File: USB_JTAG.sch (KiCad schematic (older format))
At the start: 31 parts, among them J4 USB_B_Micro, J5 AVR-JTAG-10, U11 5M1270ZT144C5N, U12 93LC46BT-I/OT, U8 FT2232H, U9 TPD2EUSB30, X1 KC5032K12.0000C10E00

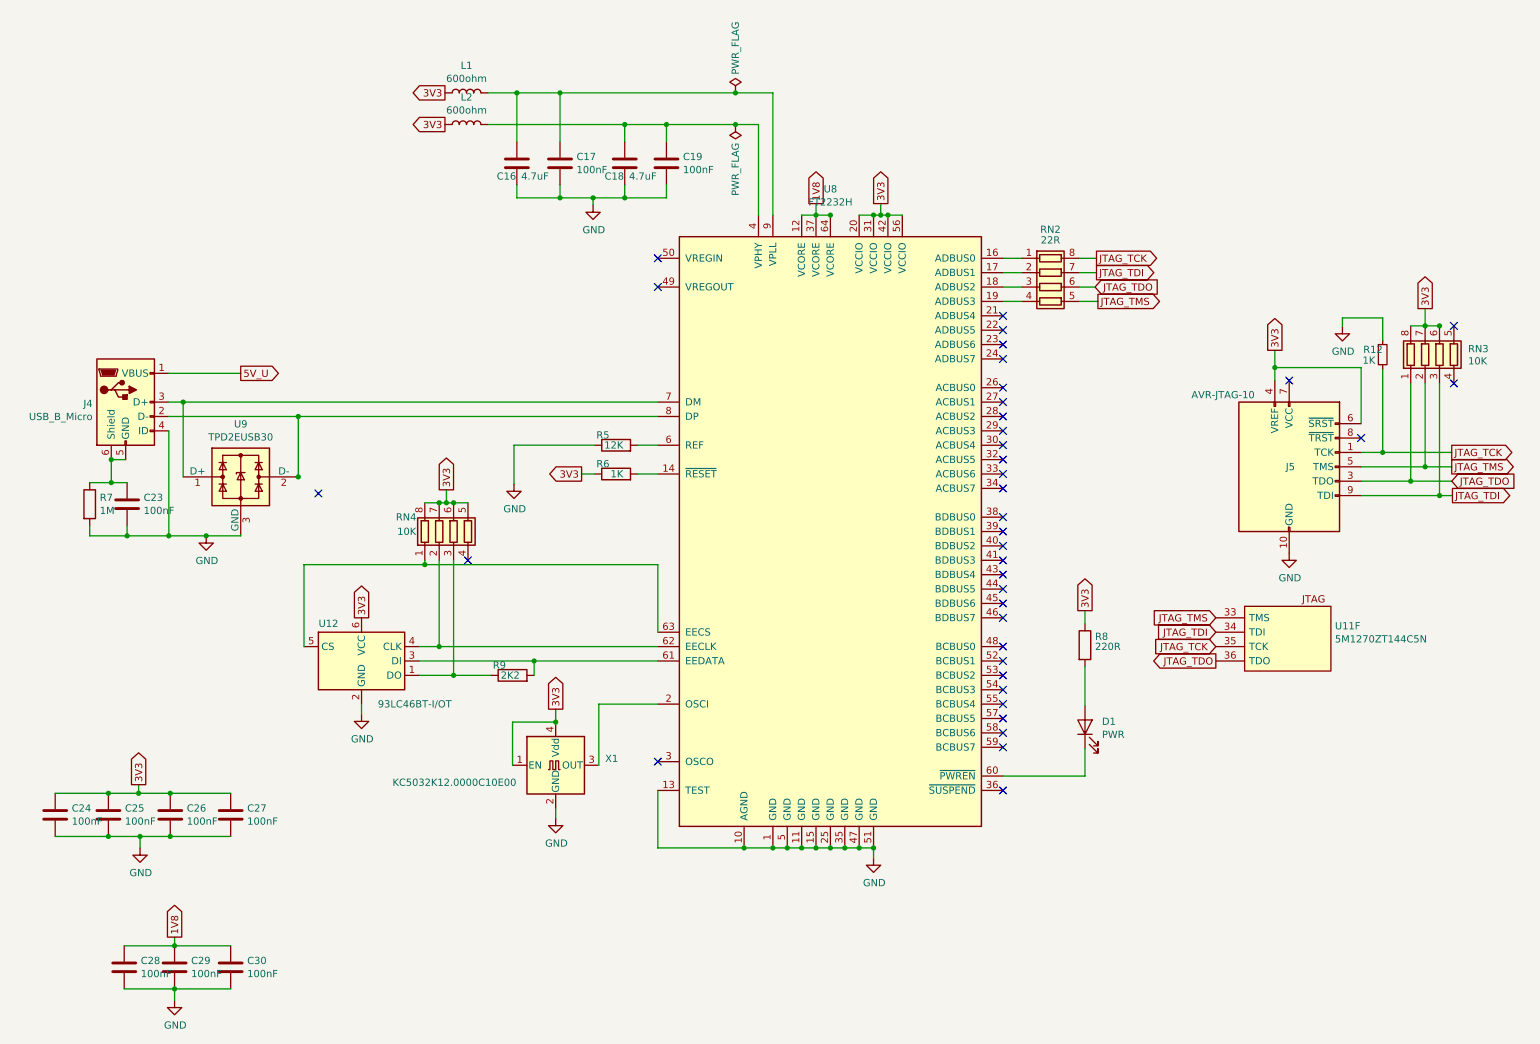
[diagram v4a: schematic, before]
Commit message: replaced some global pins with hierarchical sheet pins
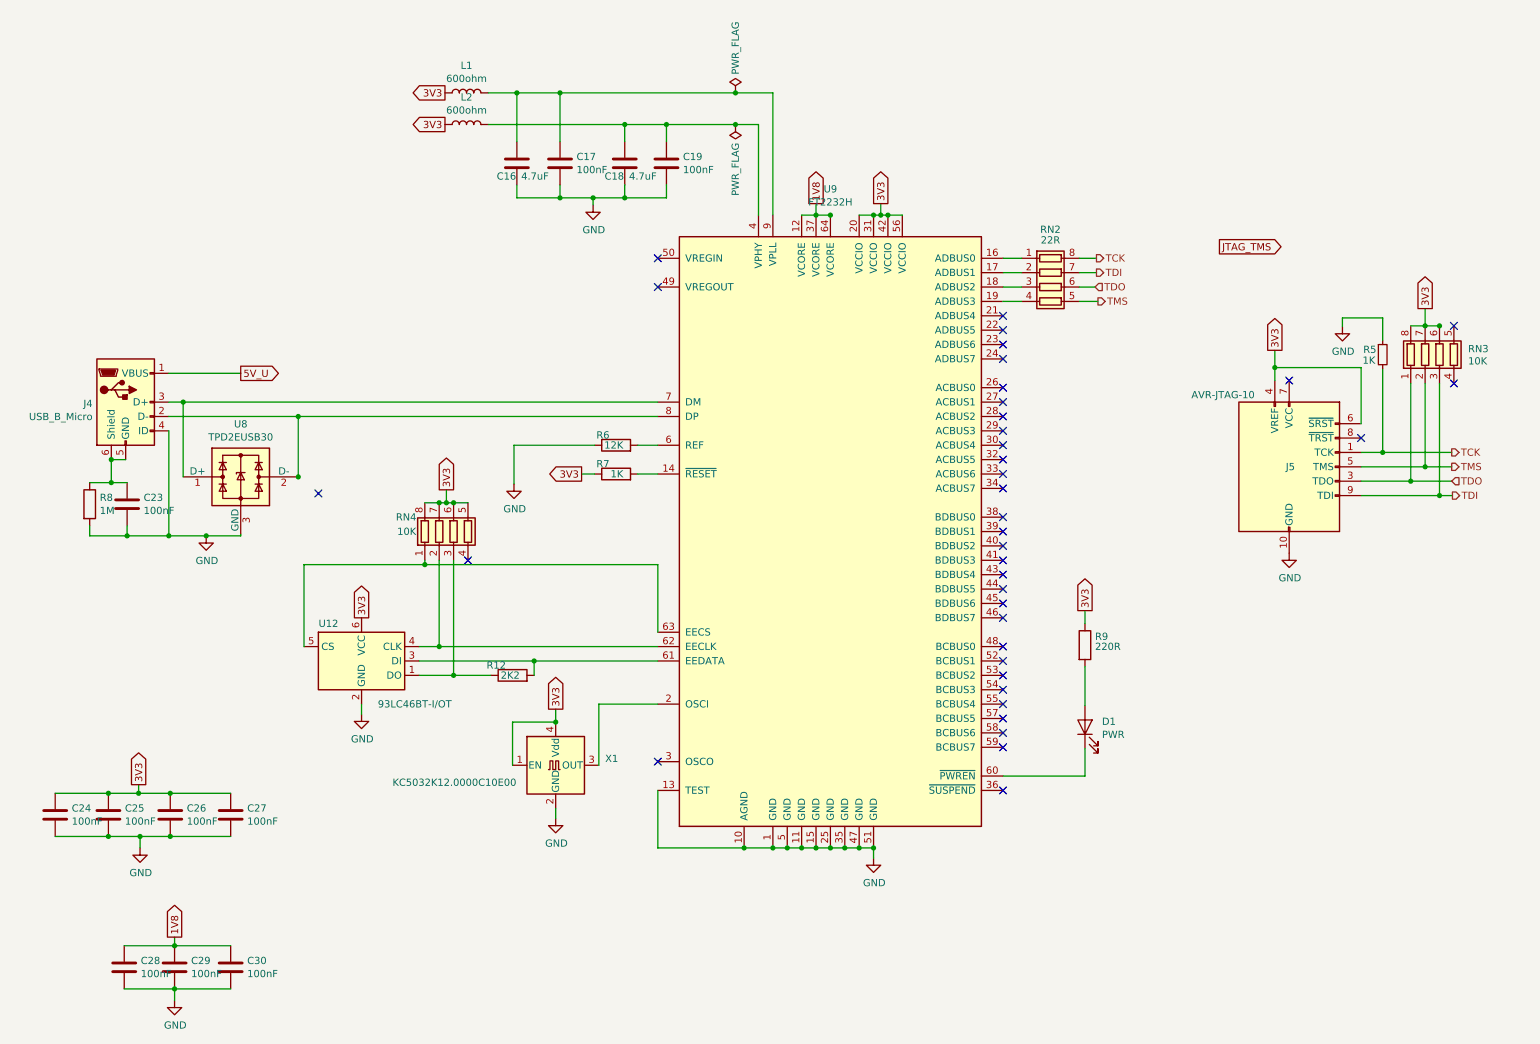
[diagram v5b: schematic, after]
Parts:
- removed U11: 5M1270ZT144C5N, Package_QFP:TQFP-144_20x20mm_P0.5mm, symbol rc2014_max_v-rescue:5M1270ZT144C5N-CPLD_Altera
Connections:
- net JTAG_TMS: no longer J5.5 (TMS), RN2.5 (R4.2), RN3.2 (R2.1)
- net JTAG_TCK renamed TCK
- net JTAG_TDI renamed TDI
- net JTAG_TDO renamed TDO
- new net TMS: J5.5 (TMS), RN2.5 (R4.2), RN3.2 (R2.1)

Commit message: recovered layout
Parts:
- X1: symbol Oscillator:KC5032K12.0000C10E00 -> rc2014_max_v-rescue:KC5032K12.0000C10E00-Oscillator
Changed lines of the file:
@@
 	1    0    0    1
 $EndComp
-Text GLabel 8905 2050 2    50   Output ~ 0
-JTAG_TMS
 Text GLabel 2100 2930 2    50   Output ~ 0
 5V_U
@@
 NoConn ~ 5000 5630
 $Comp
-L Oscillator:KC5032K12.0000C10E00 X1
+L rc2014_max_v-rescue:KC5032K12.0000C10E00-Oscillator X1
 U 1 1 5D18454F
 P 4290 5655
 AR Path="/5D0F9837/5D18454F" Ref="X1"  Part="1"
 AR Path="/5CFABACD/5D0BF766/5D18454F" Ref="X1"  Part="1"
+AR Path="/5D18454F" Ref="X1"  Part="1"
 F 0 "X1" H 4634 5701 50  0000 L CNN
 F 1 "KC5032K12.0000C10E00" H 3155 5535 50  0000 L CNN

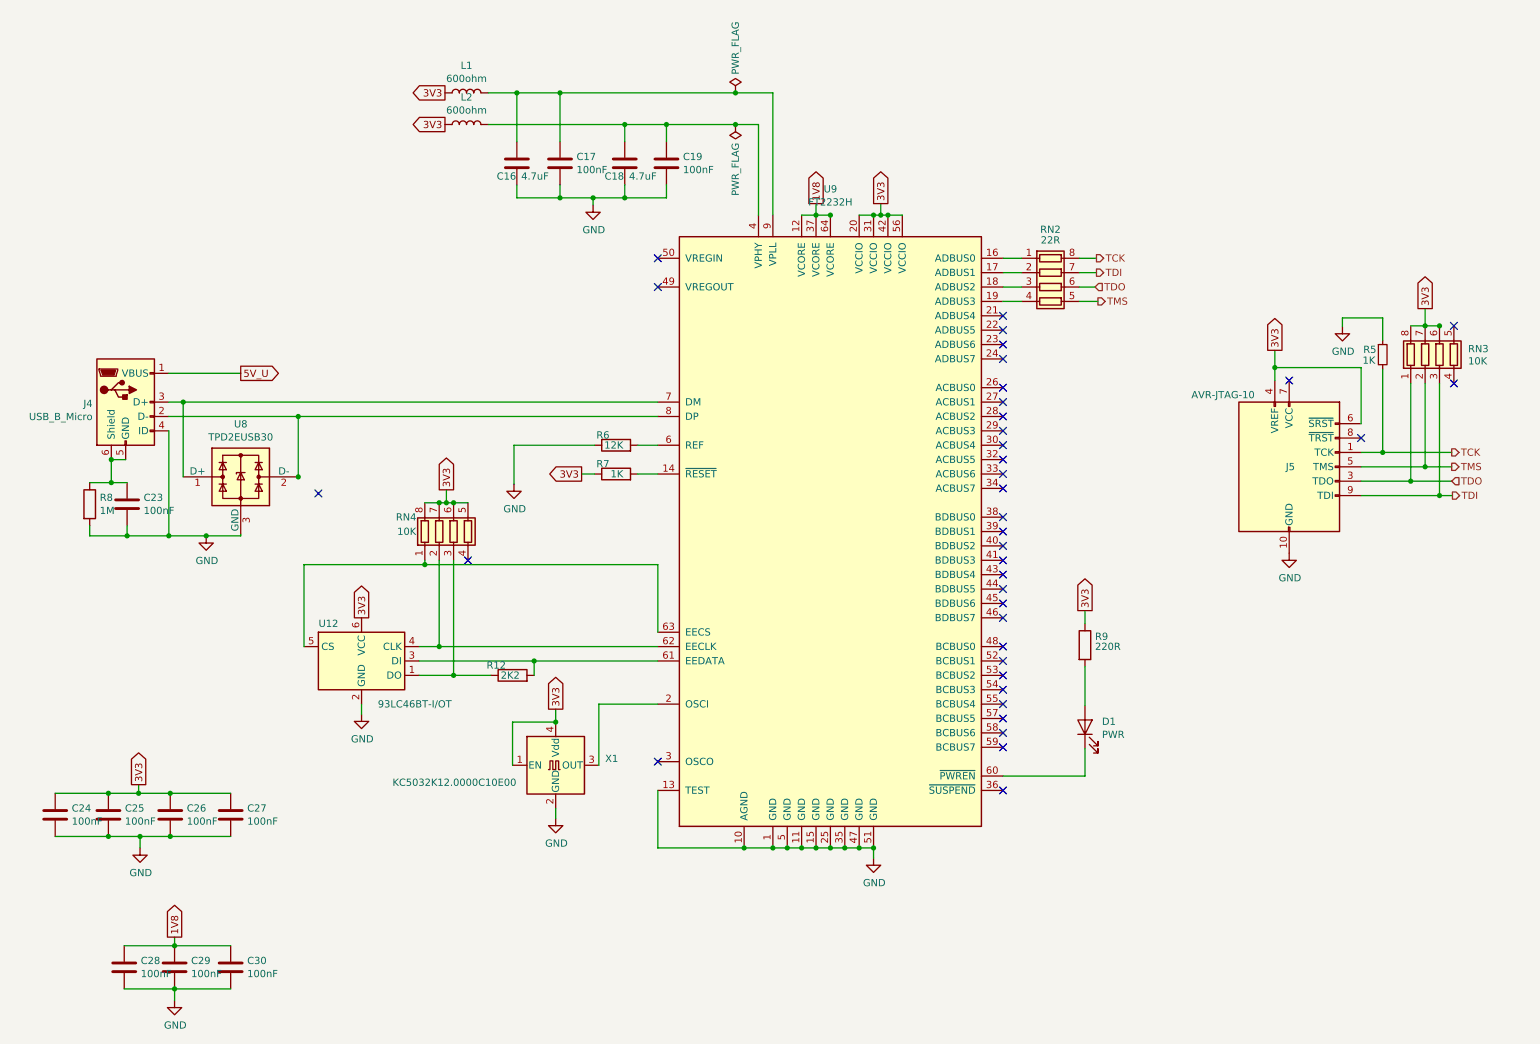
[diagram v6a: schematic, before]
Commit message: Added bus structure, additional pins added, 5V load balancer
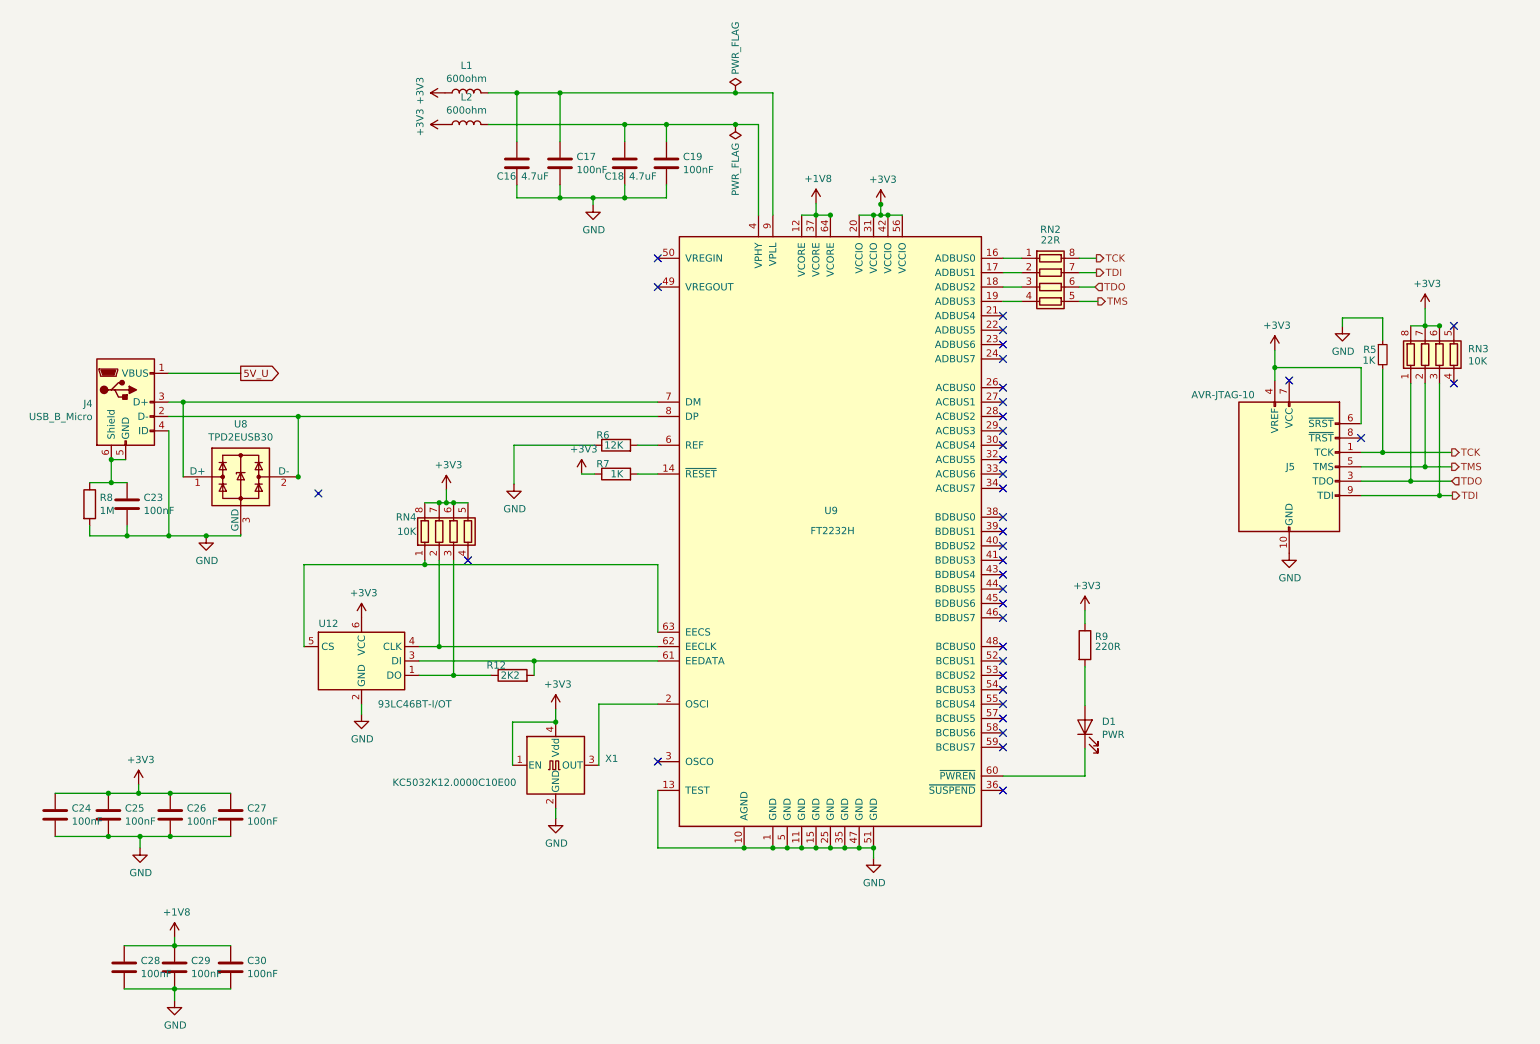
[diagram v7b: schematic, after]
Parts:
- J5: footprint Connector_IDC:IDC-Header_2x05_P2.54mm_Horizontal -> Connector_PinHeader_1.27mm:PinHeader_2x05_P1.27mm_Vertical
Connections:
- net labels added: +1V8, +3V3
- net labels removed: 1V8, 3V3
- wire segments 145 -> 146
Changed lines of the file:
@@
 EESchema Schematic File Version 4
 LIBS:rc2014_max_v-cache
+LIBS:sbc_z80-cache
+LIBS:power_share-cache
 EELAYER 29 0
 EELAYER END
@@
 F 0 "J5" H 9430 3580 50  0000 R CNN
 F 1 "AVR-JTAG-10" H 9150 4080 50  0000 R CNN
-F 2 "Connector_IDC:IDC-Header_2x05_P2.54mm_Horizontal" V 9240 3730 50  0001 C CNN
+F 2 "Connector_PinHeader_1.27mm:PinHeader_2x05_P1.27mm_Vertical" V 9240 3730 50  0001 C CNN
 F 3 "~" H 8115 3030 50  0001 C CNN
 	1    9390 3580
@@
 AR Path="/5D0F9837/5D013565" Ref="U8"  Part="1"
 AR Path="/5CFABACD/5D0BF766/5D013565" Ref="U9"  Part="1"
-F 0 "U9" H 6200 6411 50  0000 C CNN
-F 1 "FT2232H" H 6200 6320 50  0000 C CNN
+F 0 "U9" H 6205 4175 50  0000 C CNN
+F 1 "FT2232H" H 6215 4035 50  0000 C CNN
 F 2 "Package_QFP:TQFP-64_10x10mm_P0.5mm" H 6200 4030 50  0001 C CNN
 F 3 "https://www.mouser.com/datasheet/2/163/DS_FT2232H-17353.pdf" H 6200 4030 50  0001 C CNN
@@
 Text GLabel 2100 2930 2    50   Output ~ 0
 5V_U
-Text GLabel 6550 1750 1    50   Output ~ 0
-3V3
-Text GLabel 6100 1750 1    50   Output ~ 0
-1V8
-Text GLabel 3520 980  0    50   Output ~ 0
-3V3
-Text GLabel 3520 1200 0    50   Output ~ 0
-3V3
-Text GLabel 3530 3740 1    50   Output ~ 0
-3V3
-Text GLabel 10335 2480 1    50   Output ~ 0
-3V3
-Text GLabel 9290 2770 1    50   Output ~ 0
-3V3
-Text GLabel 7970 4580 1    50   Output ~ 0
-3V3
-Text GLabel 1390 5790 1    50   Output ~ 0
-3V3
-Text GLabel 1640 6850 1    50   Output ~ 0
-1V8
-Text GLabel 2940 4630 1    50   Output ~ 0
-3V3
-Text GLabel 4470 3630 0    50   Output ~ 0
-3V3
 Wire Wire Line
 	5000 5830 5000 6230
@@
 	6100 1830 6100 1750
 Wire Wire Line
-	6550 1830 6550 1750
+	6550 1830 6550 1755
 Wire Wire Line
 	1600 3130 1700 3130
@@
 Wire Wire Line
 	3990 5355 4290 5355
-Text GLabel 4290 5265 1    50   Output ~ 0
-3V3
 Wire Wire Line
 	4290 5265 4290 5355
@@
 Text HLabel 10520 3580 2    50   Output ~ 0
 TMS
+$Comp
+L power:+3V3 #PWR?
+U 1 1 5D9343EB
+P 4470 3630
+AR Path="/5D9343EB" Ref="#PWR?"  Part="1"
+AR Path="/5CFABACD/5D0BF766/5D9343EB" Ref="#PWR060"  Part="1"
+F 0 "#PWR060" H 4470 3480 50  0001 C CNN
+F 1 "+3V3" H 4485 3803 50  0000 C CNN
+F 2 "" H 4470 3630 50  0001 C CNN
+F 3 "" H 4470 3630 50  0001 C CNN
+	1    4470 3630
+	1    0    0    -1
+$EndComp
+$Comp
+L power:+3V3 #PWR?
+U 1 1 5D94566F
+P 3530 3740
+AR Path="/5D94566F" Ref="#PWR?"  Part="1"
+AR Path="/5CFABACD/5D0BF766/5D94566F" Ref="#PWR062"  Part="1"
+F 0 "#PWR062" H 3530 3590 50  0001 C CNN
+F 1 "+3V3" H 3545 3913 50  0000 C CNN
+F 2 "" H 3530 3740 50  0001 C CNN
+F 3 "" H 3530 3740 50  0001 C CNN
+	1    3530 3740
+	1    0    0    -1
+$EndComp
+$Comp
+L power:+3V3 #PWR?
+U 1 1 5D956672
+P 2940 4630
+AR Path="/5D956672" Ref="#PWR?"  Part="1"
+AR Path="/5CFABACD/5D0BF766/5D956672" Ref="#PWR064"  Part="1"
+F 0 "#PWR064" H 2940 4480 50  0001 C CNN
+F 1 "+3V3" H 2955 4803 50  0000 C CNN
+F 2 "" H 2940 4630 50  0001 C CNN
+F 3 "" H 2940 4630 50  0001 C CNN
+	1    2940 4630
+	1    0    0    -1
+$EndComp
+$Comp
+L power:+3V3 #PWR?
+U 1 1 5D9675DE
+P 4290 5265
+AR Path="/5D9675DE" Ref="#PWR?"  Part="1"
+AR Path="/5CFABACD/5D0BF766/5D9675DE" Ref="#PWR065"  Part="1"
+F 0 "#PWR065" H 4290 5115 50  0001 C CNN
+F 1 "+3V3" H 4305 5438 50  0000 C CNN
+F 2 "" H 4290 5265 50  0001 C CNN
+F 3 "" H 4290 5265 50  0001 C CNN
+	1    4290 5265
+	1    0    0    -1
+$EndComp
+$Comp
+L power:+3V3 #PWR?
+U 1 1 5D9784C6
+P 1390 5790
+AR Path="/5D9784C6" Ref="#PWR?"  Part="1"
+AR Path="/5CFABACD/5D0BF766/5D9784C6" Ref="#PWR067"  Part="1"
+F 0 "#PWR067" H 1390 5640 50  0001 C CNN
+F 1 "+3V3" H 1405 5963 50  0000 C CNN
+F 2 "" H 1390 5790 50  0001 C CNN
+F 3 "" H 1390 5790 50  0001 C CNN
+	1    1390 5790
+	1    0    0    -1
+$EndComp
+$Comp
+L power:+1V8 #PWR068
+U 1 1 5D9891A4
+P 1640 6850
+F 0 "#PWR068" H 1640 6700 50  0001 C CNN
+F 1 "+1V8" H 1655 7023 50  0000 C CNN
+F 2 "" H 1640 6850 50  0001 C CNN
+F 3 "" H 1640 6850 50  0001 C CNN
+	1    1640 6850
+	1    0    0    -1
+$EndComp
+$Comp
+L power:+3V3 #PWR?
+U 1 1 5D995718
+P 6550 1755
+AR Path="/5D995718" Ref="#PWR?"  Part="1"
+AR Path="/5CFABACD/5D0BF766/5D995718" Ref="#PWR057"  Part="1"
+F 0 "#PWR057" H 6550 1605 50  0001 C CNN
+F 1 "+3V3" H 6565 1928 50  0000 C CNN
+F 2 "" H 6550 1755 50  0001 C CNN
+F 3 "" H 6550 1755 50  0001 C CNN
+	1    6550 1755
+	1    0    0    -1
+$EndComp
+Connection ~ 6550 1755
+Wire Wire Line
+	6550 1755 6550 1750
+$Comp
+L power:+3V3 #PWR?
+U 1 1 5D9AC54D
+P 9290 2770
+AR Path="/5D9AC54D" Ref="#PWR?"  Part="1"
+AR Path="/5CFABACD/5D0BF766/5D9AC54D" Ref="#PWR059"  Part="1"
+F 0 "#PWR059" H 9290 2620 50  0001 C CNN
+F 1 "+3V3" H 9305 2943 50  0000 C CNN
+F 2 "" H 9290 2770 50  0001 C CNN
+F 3 "" H 9290 2770 50  0001 C CNN
+	1    9290 2770
+	1    0    0    -1
+$EndComp
+$Comp
+L power:+3V3 #PWR?
+U 1 1 5D9B1E4B
+P 10335 2480
+AR Path="/5D9B1E4B" Ref="#PWR?"  Part="1"
+AR Path="/5CFABACD/5D0BF766/5D9B1E4B" Ref="#PWR058"  Part="1"
+F 0 "#PWR058" H 10335 2330 50  0001 C CNN
+F 1 "+3V3" H 10350 2653 50  0000 C CNN
+F 2 "" H 10335 2480 50  0001 C CNN
+F 3 "" H 10335 2480 50  0001 C CNN
+	1    10335 2480
+	1    0    0    -1
+$EndComp
+$Comp
+L power:+3V3 #PWR?
+U 1 1 5D9D4519
+P 3520 980
+AR Path="/5D9D4519" Ref="#PWR?"  Part="1"
+AR Path="/5CFABACD/5D0BF766/5D9D4519" Ref="#PWR054"  Part="1"
+F 0 "#PWR054" H 3520 830 50  0001 C CNN
+F 1 "+3V3" H 3535 1153 50  0000 C CNN
+F 2 "" H 3520 980 50  0001 C CNN
+F 3 "" H 3520 980 50  0001 C CNN
+	1    3520 980
+	0    -1   -1   0
+$EndComp
+$Comp
+L power:+3V3 #PWR?
+U 1 1 5D9DFE3B
+P 3520 1200
+AR Path="/5D9DFE3B" Ref="#PWR?"  Part="1"
+AR Path="/5CFABACD/5D0BF766/5D9DFE3B" Ref="#PWR055"  Part="1"
+F 0 "#PWR055" H 3520 1050 50  0001 C CNN
+F 1 "+3V3" H 3535 1373 50  0000 C CNN
+F 2 "" H 3520 1200 50  0001 C CNN
+F 3 "" H 3520 1200 50  0001 C CNN
+	1    3520 1200
+	0    -1   -1   0
+$EndComp
+$Comp
+L power:+1V8 #PWR056
+U 1 1 5D9EC038
+P 6100 1750
+F 0 "#PWR056" H 6100 1600 50  0001 C CNN
+F 1 "+1V8" H 6115 1923 50  0000 C CNN
+F 2 "" H 6100 1750 50  0001 C CNN
+F 3 "" H 6100 1750 50  0001 C CNN
+	1    6100 1750
+	1    0    0    -1
+$EndComp
+$Comp
+L power:+3V3 #PWR?
+U 1 1 5D9F9447
+P 7970 4580
+AR Path="/5D9F9447" Ref="#PWR?"  Part="1"
+AR Path="/5CFABACD/5D0BF766/5D9F9447" Ref="#PWR063"  Part="1"
+F 0 "#PWR063" H 7970 4430 50  0001 C CNN
+F 1 "+3V3" H 7985 4753 50  0000 C CNN
+F 2 "" H 7970 4580 50  0001 C CNN
+F 3 "" H 7970 4580 50  0001 C CNN
+	1    7970 4580
+	1    0    0    -1
+$EndComp
 $EndSCHEMATC
